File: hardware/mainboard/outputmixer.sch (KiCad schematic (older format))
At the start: 13 parts, among them U15 TL072

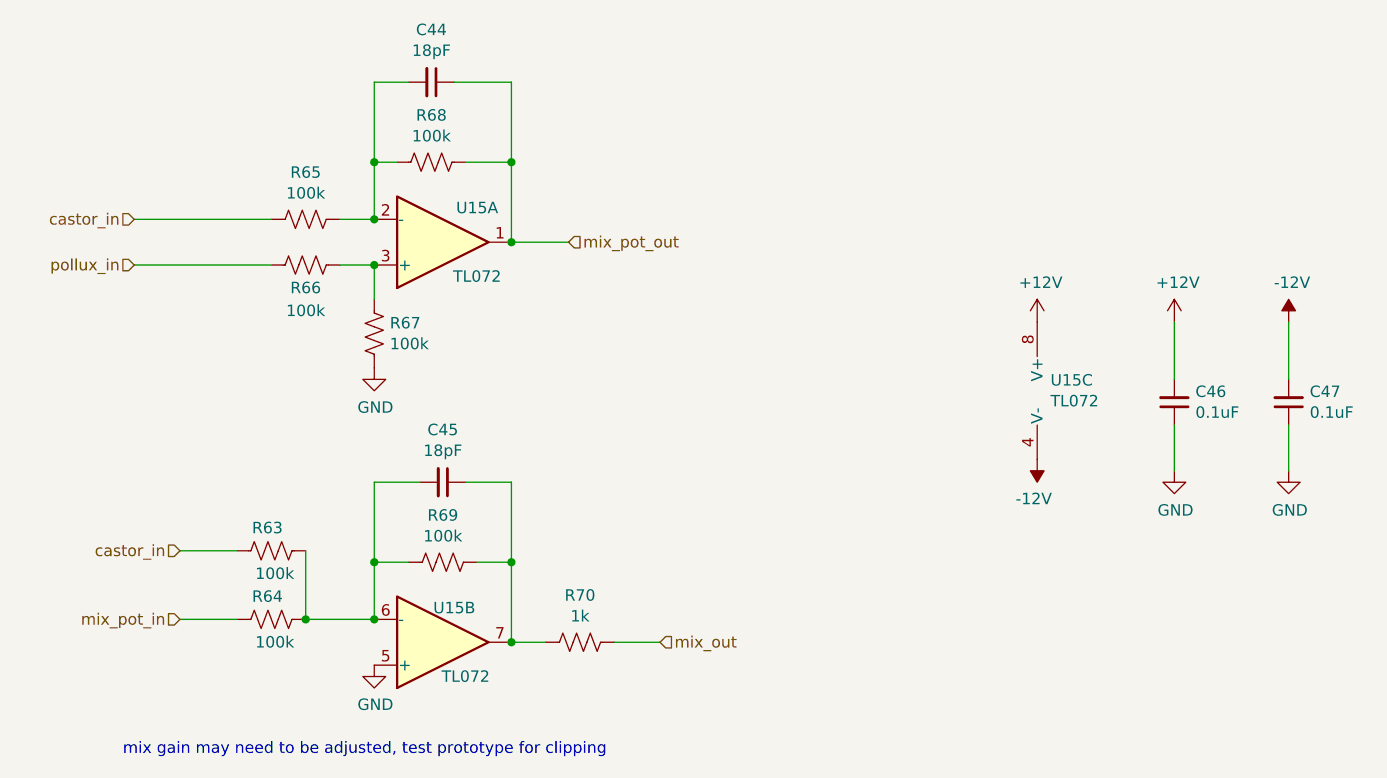
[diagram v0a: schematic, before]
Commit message: Cleanup some comments in the schematic
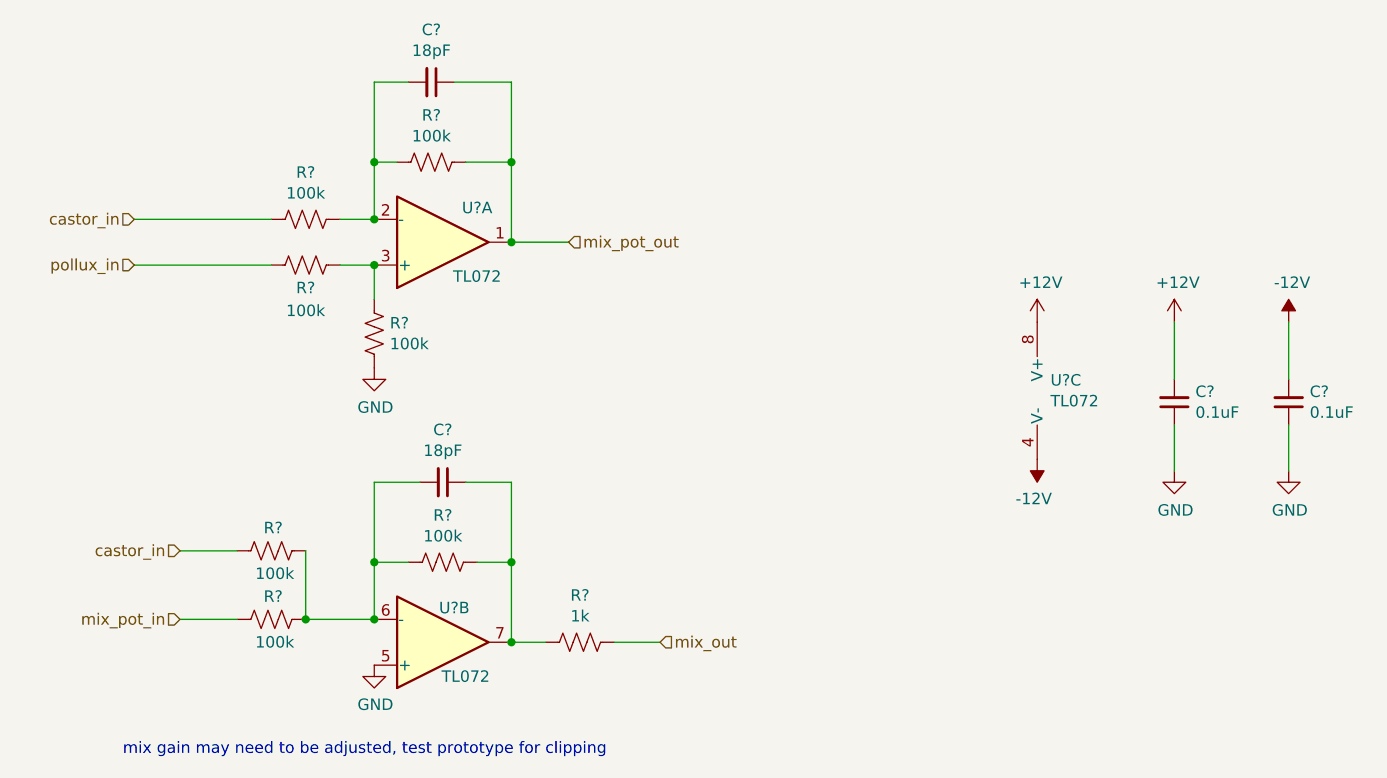
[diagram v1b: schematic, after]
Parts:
- renumbered C44 to C?, C45 to C?, C46 to C?, C47 to C?, R65 to R?, R66 to R?, R67 to R?, R68 to R?, R63 to R?, R64 to R?, R69 to R?, R70 to R?, U15 to U?
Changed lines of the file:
@@
 $EndDescr
 $Comp
-L Amplifier_Operational:TL072 U15
+L Amplifier_Operational:TL072 U?
 U 2 1 5F4288B5
 P 3400 4150
-F 0 "U15" H 3450 4000 50  0000 C CNN
+F 0 "U?" H 3450 4000 50  0000 C CNN
 F 1 "TL072" H 3500 4300 50  0000 C CNN
 F 2 "Package_SO:TSSOP-8_4.4x3mm_P0.65mm" H 3400 4150 50  0001 C CNN
@@
 $EndComp
 $Comp
-L Amplifier_Operational:TL072 U15
+L Amplifier_Operational:TL072 U?
 U 3 1 5F42A9BD
 P 6100 3050
-F 0 "U15" H 6058 3096 50  0000 L CNN
+F 0 "U?" H 6058 3096 50  0000 L CNN
 F 1 "TL072" H 6058 3005 50  0000 L CNN
 F 2 "Package_SO:TSSOP-8_4.4x3mm_P0.65mm" H 6100 3050 50  0001 C CNN
@@
 $EndComp
 $Comp
-L Device:R_US R65
+L Device:R_US R?
 U 1 1 5F42DF85
 P 2800 2300
-F 0 "R65" V 2595 2300 50  0000 C CNN
+F 0 "R?" V 2595 2300 50  0000 C CNN
 F 1 "100k" V 2686 2300 50  0000 C CNN
 F 2 "Resistor_SMD:R_0603_1608Metric_Pad1.05x0.95mm_HandSolder" V 2840 2290 50  0001 C CNN
@@
 pollux_in
 $Comp
-L Device:R_US R66
+L Device:R_US R?
 U 1 1 5F42F7A8
 P 2800 2500
-F 0 "R66" V 2900 2500 50  0000 C CNN
+F 0 "R?" V 2900 2500 50  0000 C CNN
 F 1 "100k" V 3000 2500 50  0000 C CNN
 F 2 "Resistor_SMD:R_0603_1608Metric_Pad1.05x0.95mm_HandSolder" V 2840 2490 50  0001 C CNN
@@
 $EndComp
 $Comp
-L Device:R_US R67
+L Device:R_US R?
 U 1 1 5F430473
 P 3100 2800
-F 0 "R67" H 3032 2754 50  0000 R CNN
+F 0 "R?" H 3032 2754 50  0000 R CNN
 F 1 "100k" H 3032 2845 50  0000 R CNN
 F 2 "Resistor_SMD:R_0603_1608Metric_Pad1.05x0.95mm_HandSolder" V 3140 2790 50  0001 C CNN
@@
 $EndComp
 $Comp
-L Amplifier_Operational:TL072 U15
+L Amplifier_Operational:TL072 U?
 U 1 1 5F422A70
 P 3400 2400
-F 0 "U15" H 3550 2250 50  0000 C CNN
+F 0 "U?" H 3550 2250 50  0000 C CNN
 F 1 "TL072" H 3550 2550 50  0000 C CNN
 F 2 "Package_SO:TSSOP-8_4.4x3mm_P0.65mm" H 3400 2400 50  0001 C CNN
@@
 $EndComp
 $Comp
-L Device:R_US R68
+L Device:R_US R?
 U 1 1 5F43223D
 P 3350 2050
-F 0 "R68" V 3555 2050 50  0000 C CNN
+F 0 "R?" V 3555 2050 50  0000 C CNN
 F 1 "100k" V 3464 2050 50  0000 C CNN
 F 2 "Resistor_SMD:R_0603_1608Metric_Pad1.05x0.95mm_HandSolder" V 3390 2040 50  0001 C CNN
@@
 	3700 2050 3700 2400
 $Comp
-L Device:R_US R63
+L Device:R_US R?
 U 1 1 5F437861
 P 2650 3750
-F 0 "R63" V 2750 3700 50  0000 L CNN
+F 0 "R?" V 2750 3700 50  0000 L CNN
 F 1 "100k" V 2550 3650 50  0000 L CNN
 F 2 "Resistor_SMD:R_0603_1608Metric_Pad1.05x0.95mm_HandSolder" V 2690 3740 50  0001 C CNN
@@
 $EndComp
 $Comp
-L Device:C_Small C44
+L Device:C_Small C?
 U 1 1 5F43967E
 P 3350 1700
-F 0 "C44" V 3121 1700 50  0000 C CNN
+F 0 "C?" V 3121 1700 50  0000 C CNN
 F 1 "18pF" V 3212 1700 50  0000 C CNN
 F 2 "Capacitor_SMD:C_0603_1608Metric_Pad1.05x0.95mm_HandSolder" H 3350 1700 50  0001 C CNN
@@
 mix_pot_in
 $Comp
-L Device:R_US R64
+L Device:R_US R?
 U 1 1 5F44AC44
 P 2650 4050
-F 0 "R64" V 2750 4000 50  0000 L CNN
+F 0 "R?" V 2750 4000 50  0000 L CNN
 F 1 "100k" V 2550 3950 50  0000 L CNN
 F 2 "Resistor_SMD:R_0603_1608Metric_Pad1.05x0.95mm_HandSolder" V 2690 4040 50  0001 C CNN
@@
 Connection ~ 2800 4050
 $Comp
-L power:GND #PWR0128
+L power:GND #PWR?
 U 1 1 5F44D6B7
 P 3100 4250
-F 0 "#PWR0128" H 3100 4000 50  0001 C CNN
+F 0 "#PWR?" H 3100 4000 50  0001 C CNN
 F 1 "GND" H 3105 4077 50  0000 C CNN
 F 2 "" H 3100 4250 50  0001 C CNN
@@
 $EndComp
 $Comp
-L power:GND #PWR0129
+L power:GND #PWR?
 U 1 1 5F44DA38
 P 3100 2950
-F 0 "#PWR0129" H 3100 2700 50  0001 C CNN
+F 0 "#PWR?" H 3100 2700 50  0001 C CNN
 F 1 "GND" H 3105 2777 50  0000 C CNN
 F 2 "" H 3100 2950 50  0001 C CNN
@@
 mix_out
 $Comp
-L Device:R_US R69
+L Device:R_US R?
 U 1 1 5F44E796
 P 3400 3800
-F 0 "R69" V 3605 3800 50  0000 C CNN
+F 0 "R?" V 3605 3800 50  0000 C CNN
 F 1 "100k" V 3514 3800 50  0000 C CNN
 F 2 "Resistor_SMD:R_0603_1608Metric_Pad1.05x0.95mm_HandSolder" V 3440 3790 50  0001 C CNN
@@
 	3700 3800 3700 4150
 $Comp
-L Device:R_US R70
+L Device:R_US R?
 U 1 1 5F450B70
 P 4000 4150
-F 0 "R70" V 4205 4150 50  0000 C CNN
+F 0 "R?" V 4205 4150 50  0000 C CNN
 F 1 "1k" V 4114 4150 50  0000 C CNN
 F 2 "Resistor_SMD:R_0603_1608Metric_Pad1.05x0.95mm_HandSolder" V 4040 4140 50  0001 C CNN
@@
 	4150 4150 4350 4150
 $Comp
-L Device:C_Small C45
+L Device:C_Small C?
 U 1 1 5F45200A
 P 3400 3450
-F 0 "C45" V 3171 3450 50  0000 C CNN
+F 0 "C?" V 3171 3450 50  0000 C CNN
 F 1 "18pF" V 3262 3450 50  0000 C CNN
 F 2 "Capacitor_SMD:C_0603_1608Metric_Pad1.05x0.95mm_HandSolder" H 3400 3450 50  0001 C CNN
@@
 mix gain may need to be adjusted, test prototype for clipping
 $Comp
-L power:+12V #PWR0130
+L power:+12V #PWR?
 U 1 1 5F45598F
 P 6000 2750
-F 0 "#PWR0130" H 6000 2600 50  0001 C CNN
+F 0 "#PWR?" H 6000 2600 50  0001 C CNN
 F 1 "+12V" H 6015 2923 50  0000 C CNN
 F 2 "" H 6000 2750 50  0001 C CNN
@@
 $EndComp
 $Comp
-L power:-12V #PWR0131
+L power:-12V #PWR?
 U 1 1 5F455E26
 P 6000 3350
-F 0 "#PWR0131" H 6000 3450 50  0001 C CNN
+F 0 "#PWR?" H 6000 3450 50  0001 C CNN
 F 1 "-12V" H 6015 3523 50  0000 C CNN
 F 2 "" H 6000 3350 50  0001 C CNN
@@
 $EndComp
 $Comp
-L power:+12V #PWR0132
+L power:+12V #PWR?
 U 1 1 5F456222
 P 6600 2750
-F 0 "#PWR0132" H 6600 2600 50  0001 C CNN
+F 0 "#PWR?" H 6600 2600 50  0001 C CNN
 F 1 "+12V" H 6615 2923 50  0000 C CNN
 F 2 "" H 6600 2750 50  0001 C CNN
@@
 $EndComp
 $Comp
-L power:-12V #PWR0133
+L power:-12V #PWR?
 U 1 1 5F45684C
 P 7100 2750
-F 0 "#PWR0133" H 7100 2850 50  0001 C CNN
+F 0 "#PWR?" H 7100 2850 50  0001 C CNN
 F 1 "-12V" H 7115 2923 50  0000 C CNN
 F 2 "" H 7100 2750 50  0001 C CNN
@@
 $EndComp
 $Comp
-L Device:C_Small C46
+L Device:C_Small C?
 U 1 1 5F4571B8
 P 6600 3100
-F 0 "C46" H 6508 3054 50  0000 R CNN
+F 0 "C?" H 6508 3054 50  0000 R CNN
 F 1 "0.1uF" H 6508 3145 50  0000 R CNN
 F 2 "Capacitor_SMD:C_0603_1608Metric_Pad1.05x0.95mm_HandSolder" H 6600 3100 50  0001 C CNN
@@
 $EndComp
 $Comp
-L Device:C_Small C47
+L Device:C_Small C?
 U 1 1 5F4578C6
 P 7100 3100
-F 0 "C47" H 7008 3054 50  0000 R CNN
+F 0 "C?" H 7008 3054 50  0000 R CNN
 F 1 "0.1uF" H 7008 3145 50  0000 R CNN
 F 2 "Capacitor_SMD:C_0603_1608Metric_Pad1.05x0.95mm_HandSolder" H 7100 3100 50  0001 C CNN
@@
 $EndComp
 $Comp
-L power:GND #PWR0134
+L power:GND #PWR?
 U 1 1 5F457B98
 P 6600 3400
-F 0 "#PWR0134" H 6600 3150 50  0001 C CNN
+F 0 "#PWR?" H 6600 3150 50  0001 C CNN
 F 1 "GND" H 6605 3227 50  0000 C CNN
 F 2 "" H 6600 3400 50  0001 C CNN
@@
 $EndComp
 $Comp
-L power:GND #PWR0135
+L power:GND #PWR?
 U 1 1 5F458020
 P 7100 3400
-F 0 "#PWR0135" H 7100 3150 50  0001 C CNN
+F 0 "#PWR?" H 7100 3150 50  0001 C CNN
 F 1 "GND" H 7105 3227 50  0000 C CNN
 F 2 "" H 7100 3400 50  0001 C CNN

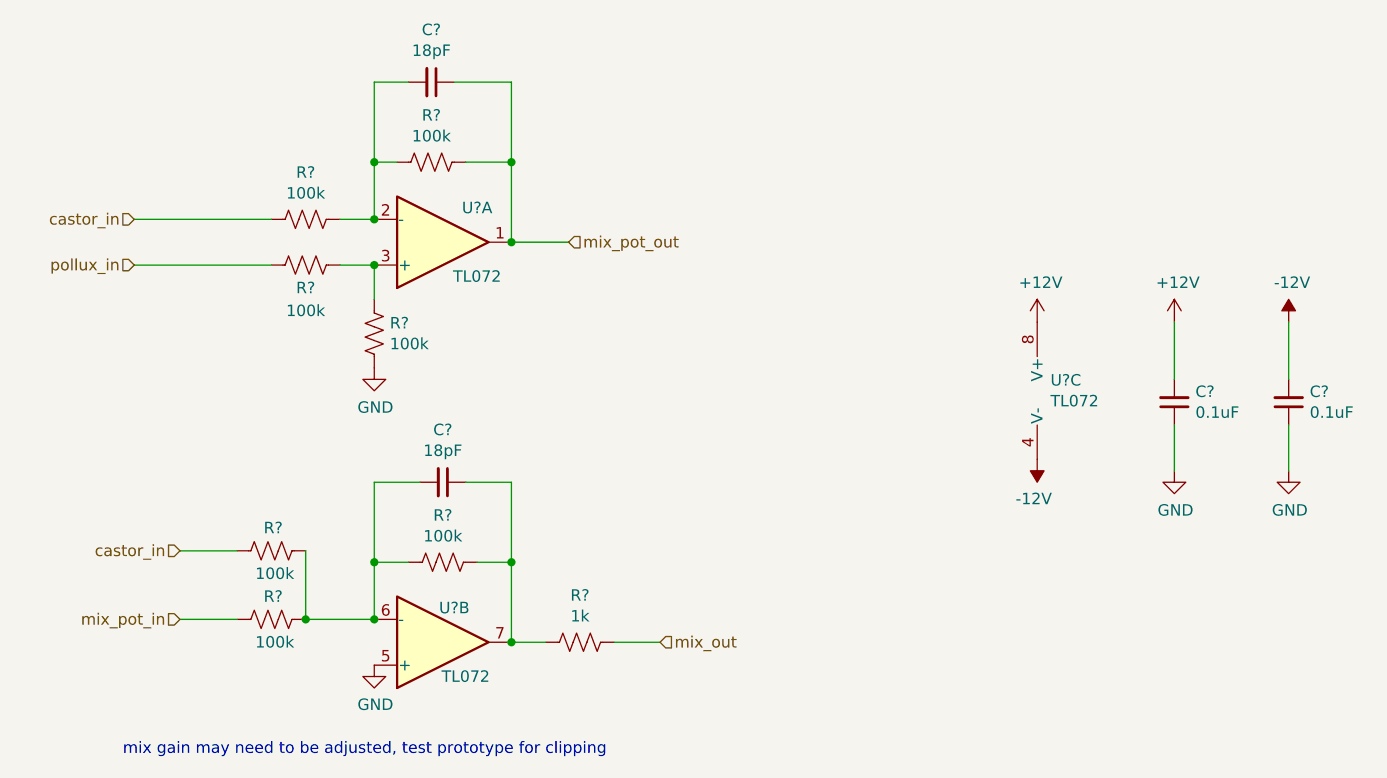
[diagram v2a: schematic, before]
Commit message: hardware: finalize BOM for v3, change 200kOhm resistors to 0603.
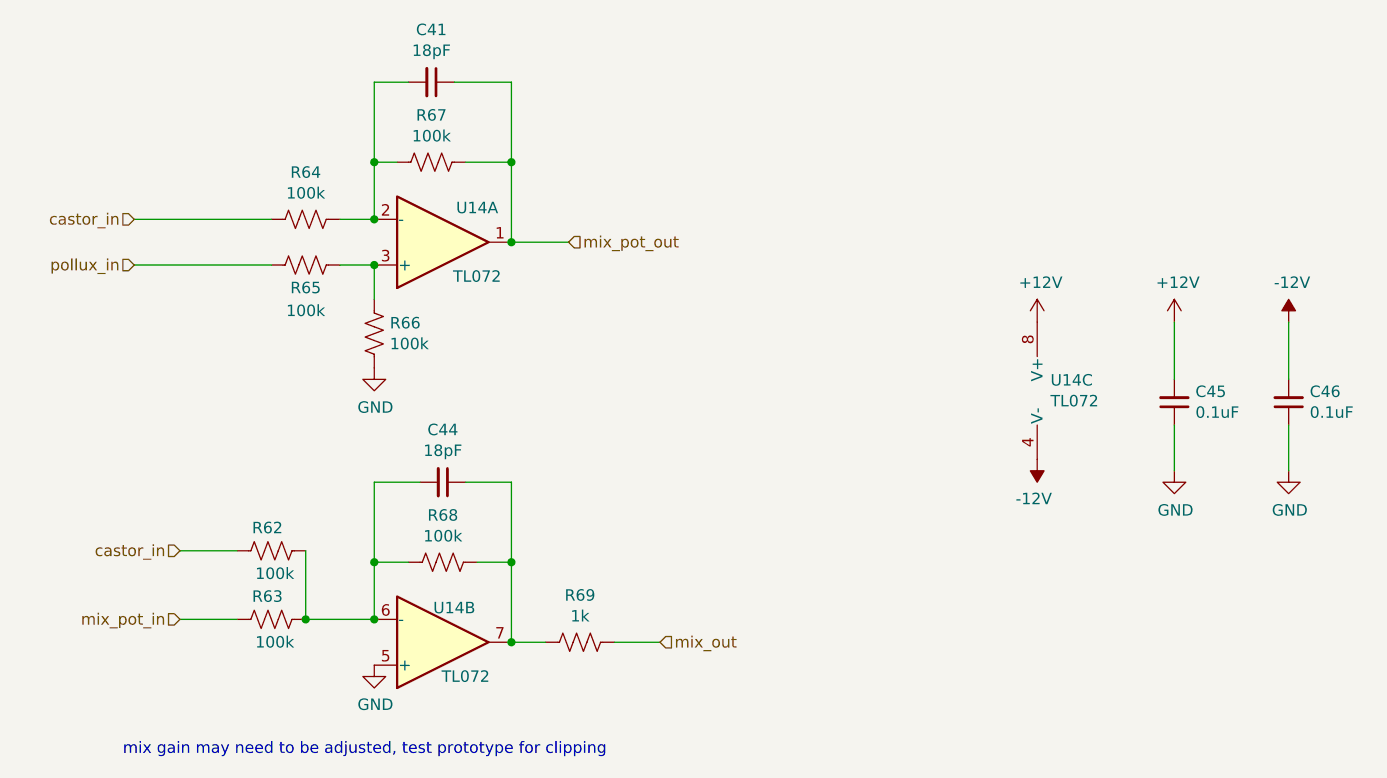
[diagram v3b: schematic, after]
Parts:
- gave numbers to parts that had none: 13
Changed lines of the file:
@@
 Sheet 3 7
 Title "Castor & Pollux"
-Date "2021-01-27"
+Date "2021-02-01"
 Rev "v3"
 Comp "Winterbloom"
@@
 $EndDescr
 $Comp
-L Amplifier_Operational:TL072 U?
+L Amplifier_Operational:TL072 U14
 U 2 1 5F4288B5
 P 3400 4150
-F 0 "U?" H 3450 4000 50  0000 C CNN
+F 0 "U14" H 3450 4000 50  0000 C CNN
 F 1 "TL072" H 3500 4300 50  0000 C CNN
 F 2 "Package_SO:TSSOP-8_4.4x3mm_P0.65mm" H 3400 4150 50  0001 C CNN
@@
 $EndComp
 $Comp
-L Amplifier_Operational:TL072 U?
+L Amplifier_Operational:TL072 U14
 U 3 1 5F42A9BD
 P 6100 3050
-F 0 "U?" H 6058 3096 50  0000 L CNN
+F 0 "U14" H 6058 3096 50  0000 L CNN
 F 1 "TL072" H 6058 3005 50  0000 L CNN
 F 2 "Package_SO:TSSOP-8_4.4x3mm_P0.65mm" H 6100 3050 50  0001 C CNN
@@
 $EndComp
 $Comp
-L Device:R_US R?
+L Device:R_US R64
 U 1 1 5F42DF85
 P 2800 2300
-F 0 "R?" V 2595 2300 50  0000 C CNN
+F 0 "R64" V 2595 2300 50  0000 C CNN
 F 1 "100k" V 2686 2300 50  0000 C CNN
 F 2 "Resistor_SMD:R_0603_1608Metric_Pad1.05x0.95mm_HandSolder" V 2840 2290 50  0001 C CNN
@@
 pollux_in
 $Comp
-L Device:R_US R?
+L Device:R_US R65
 U 1 1 5F42F7A8
 P 2800 2500
-F 0 "R?" V 2900 2500 50  0000 C CNN
+F 0 "R65" V 2900 2500 50  0000 C CNN
 F 1 "100k" V 3000 2500 50  0000 C CNN
 F 2 "Resistor_SMD:R_0603_1608Metric_Pad1.05x0.95mm_HandSolder" V 2840 2490 50  0001 C CNN
@@
 $EndComp
 $Comp
-L Device:R_US R?
+L Device:R_US R66
 U 1 1 5F430473
 P 3100 2800
-F 0 "R?" H 3032 2754 50  0000 R CNN
+F 0 "R66" H 3032 2754 50  0000 R CNN
 F 1 "100k" H 3032 2845 50  0000 R CNN
 F 2 "Resistor_SMD:R_0603_1608Metric_Pad1.05x0.95mm_HandSolder" V 3140 2790 50  0001 C CNN
@@
 $EndComp
 $Comp
-L Amplifier_Operational:TL072 U?
+L Amplifier_Operational:TL072 U14
 U 1 1 5F422A70
 P 3400 2400
-F 0 "U?" H 3550 2250 50  0000 C CNN
+F 0 "U14" H 3550 2250 50  0000 C CNN
 F 1 "TL072" H 3550 2550 50  0000 C CNN
 F 2 "Package_SO:TSSOP-8_4.4x3mm_P0.65mm" H 3400 2400 50  0001 C CNN
@@
 $EndComp
 $Comp
-L Device:R_US R?
+L Device:R_US R67
 U 1 1 5F43223D
 P 3350 2050
-F 0 "R?" V 3555 2050 50  0000 C CNN
+F 0 "R67" V 3555 2050 50  0000 C CNN
 F 1 "100k" V 3464 2050 50  0000 C CNN
 F 2 "Resistor_SMD:R_0603_1608Metric_Pad1.05x0.95mm_HandSolder" V 3390 2040 50  0001 C CNN
@@
 	3700 2050 3700 2400
 $Comp
-L Device:R_US R?
+L Device:R_US R62
 U 1 1 5F437861
 P 2650 3750
-F 0 "R?" V 2750 3700 50  0000 L CNN
+F 0 "R62" V 2750 3700 50  0000 L CNN
 F 1 "100k" V 2550 3650 50  0000 L CNN
 F 2 "Resistor_SMD:R_0603_1608Metric_Pad1.05x0.95mm_HandSolder" V 2690 3740 50  0001 C CNN
@@
 $EndComp
 $Comp
-L Device:C_Small C?
+L Device:C_Small C41
 U 1 1 5F43967E
 P 3350 1700
-F 0 "C?" V 3121 1700 50  0000 C CNN
+F 0 "C41" V 3121 1700 50  0000 C CNN
 F 1 "18pF" V 3212 1700 50  0000 C CNN
 F 2 "Capacitor_SMD:C_0603_1608Metric_Pad1.05x0.95mm_HandSolder" H 3350 1700 50  0001 C CNN
@@
 mix_pot_in
 $Comp
-L Device:R_US R?
+L Device:R_US R63
 U 1 1 5F44AC44
 P 2650 4050
-F 0 "R?" V 2750 4000 50  0000 L CNN
+F 0 "R63" V 2750 4000 50  0000 L CNN
 F 1 "100k" V 2550 3950 50  0000 L CNN
 F 2 "Resistor_SMD:R_0603_1608Metric_Pad1.05x0.95mm_HandSolder" V 2690 4040 50  0001 C CNN
@@
 Connection ~ 2800 4050
 $Comp
-L power:GND #PWR?
+L power:GND #PWR0119
 U 1 1 5F44D6B7
 P 3100 4250
-F 0 "#PWR?" H 3100 4000 50  0001 C CNN
+F 0 "#PWR0119" H 3100 4000 50  0001 C CNN
 F 1 "GND" H 3105 4077 50  0000 C CNN
 F 2 "" H 3100 4250 50  0001 C CNN
@@
 $EndComp
 $Comp
-L power:GND #PWR?
+L power:GND #PWR0120
 U 1 1 5F44DA38
 P 3100 2950
-F 0 "#PWR?" H 3100 2700 50  0001 C CNN
+F 0 "#PWR0120" H 3100 2700 50  0001 C CNN
 F 1 "GND" H 3105 2777 50  0000 C CNN
 F 2 "" H 3100 2950 50  0001 C CNN
@@
 mix_out
 $Comp
-L Device:R_US R?
+L Device:R_US R68
 U 1 1 5F44E796
 P 3400 3800
-F 0 "R?" V 3605 3800 50  0000 C CNN
+F 0 "R68" V 3605 3800 50  0000 C CNN
 F 1 "100k" V 3514 3800 50  0000 C CNN
 F 2 "Resistor_SMD:R_0603_1608Metric_Pad1.05x0.95mm_HandSolder" V 3440 3790 50  0001 C CNN
@@
 	3700 3800 3700 4150
 $Comp
-L Device:R_US R?
+L Device:R_US R69
 U 1 1 5F450B70
 P 4000 4150
-F 0 "R?" V 4205 4150 50  0000 C CNN
+F 0 "R69" V 4205 4150 50  0000 C CNN
 F 1 "1k" V 4114 4150 50  0000 C CNN
 F 2 "Resistor_SMD:R_0603_1608Metric_Pad1.05x0.95mm_HandSolder" V 4040 4140 50  0001 C CNN
@@
 	4150 4150 4350 4150
 $Comp
-L Device:C_Small C?
+L Device:C_Small C44
 U 1 1 5F45200A
 P 3400 3450
-F 0 "C?" V 3171 3450 50  0000 C CNN
+F 0 "C44" V 3171 3450 50  0000 C CNN
 F 1 "18pF" V 3262 3450 50  0000 C CNN
 F 2 "Capacitor_SMD:C_0603_1608Metric_Pad1.05x0.95mm_HandSolder" H 3400 3450 50  0001 C CNN
@@
 mix gain may need to be adjusted, test prototype for clipping
 $Comp
-L power:+12V #PWR?
+L power:+12V #PWR0121
 U 1 1 5F45598F
 P 6000 2750
-F 0 "#PWR?" H 6000 2600 50  0001 C CNN
+F 0 "#PWR0121" H 6000 2600 50  0001 C CNN
 F 1 "+12V" H 6015 2923 50  0000 C CNN
 F 2 "" H 6000 2750 50  0001 C CNN
@@
 $EndComp
 $Comp
-L power:-12V #PWR?
+L power:-12V #PWR0128
 U 1 1 5F455E26
 P 6000 3350
-F 0 "#PWR?" H 6000 3450 50  0001 C CNN
+F 0 "#PWR0128" H 6000 3450 50  0001 C CNN
 F 1 "-12V" H 6015 3523 50  0000 C CNN
 F 2 "" H 6000 3350 50  0001 C CNN
@@
 $EndComp
 $Comp
-L power:+12V #PWR?
+L power:+12V #PWR0129
 U 1 1 5F456222
 P 6600 2750
-F 0 "#PWR?" H 6600 2600 50  0001 C CNN
+F 0 "#PWR0129" H 6600 2600 50  0001 C CNN
 F 1 "+12V" H 6615 2923 50  0000 C CNN
 F 2 "" H 6600 2750 50  0001 C CNN
@@
 $EndComp
 $Comp
-L power:-12V #PWR?
+L power:-12V #PWR0130
 U 1 1 5F45684C
 P 7100 2750
-F 0 "#PWR?" H 7100 2850 50  0001 C CNN
+F 0 "#PWR0130" H 7100 2850 50  0001 C CNN
 F 1 "-12V" H 7115 2923 50  0000 C CNN
 F 2 "" H 7100 2750 50  0001 C CNN
@@
 $EndComp
 $Comp
-L Device:C_Small C?
+L Device:C_Small C45
 U 1 1 5F4571B8
 P 6600 3100
-F 0 "C?" H 6508 3054 50  0000 R CNN
+F 0 "C45" H 6508 3054 50  0000 R CNN
 F 1 "0.1uF" H 6508 3145 50  0000 R CNN
 F 2 "Capacitor_SMD:C_0603_1608Metric_Pad1.05x0.95mm_HandSolder" H 6600 3100 50  0001 C CNN
@@
 $EndComp
 $Comp
-L Device:C_Small C?
+L Device:C_Small C46
 U 1 1 5F4578C6
 P 7100 3100
-F 0 "C?" H 7008 3054 50  0000 R CNN
+F 0 "C46" H 7008 3054 50  0000 R CNN
 F 1 "0.1uF" H 7008 3145 50  0000 R CNN
 F 2 "Capacitor_SMD:C_0603_1608Metric_Pad1.05x0.95mm_HandSolder" H 7100 3100 50  0001 C CNN
@@
 $EndComp
 $Comp
-L power:GND #PWR?
+L power:GND #PWR0131
 U 1 1 5F457B98
 P 6600 3400
-F 0 "#PWR?" H 6600 3150 50  0001 C CNN
+F 0 "#PWR0131" H 6600 3150 50  0001 C CNN
 F 1 "GND" H 6605 3227 50  0000 C CNN
 F 2 "" H 6600 3400 50  0001 C CNN
@@
 $EndComp
 $Comp
-L power:GND #PWR?
+L power:GND #PWR0132
 U 1 1 5F458020
 P 7100 3400
-F 0 "#PWR?" H 7100 3150 50  0001 C CNN
+F 0 "#PWR0132" H 7100 3150 50  0001 C CNN
 F 1 "GND" H 7105 3227 50  0000 C CNN
 F 2 "" H 7100 3400 50  0001 C CNN
